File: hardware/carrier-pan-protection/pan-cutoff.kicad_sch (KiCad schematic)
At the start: 16 parts, among them Q1 100V N-MOS, Q2 100V N-MOS, U1 LTC4368IMS-2, U2 D42V55F12 / 5577

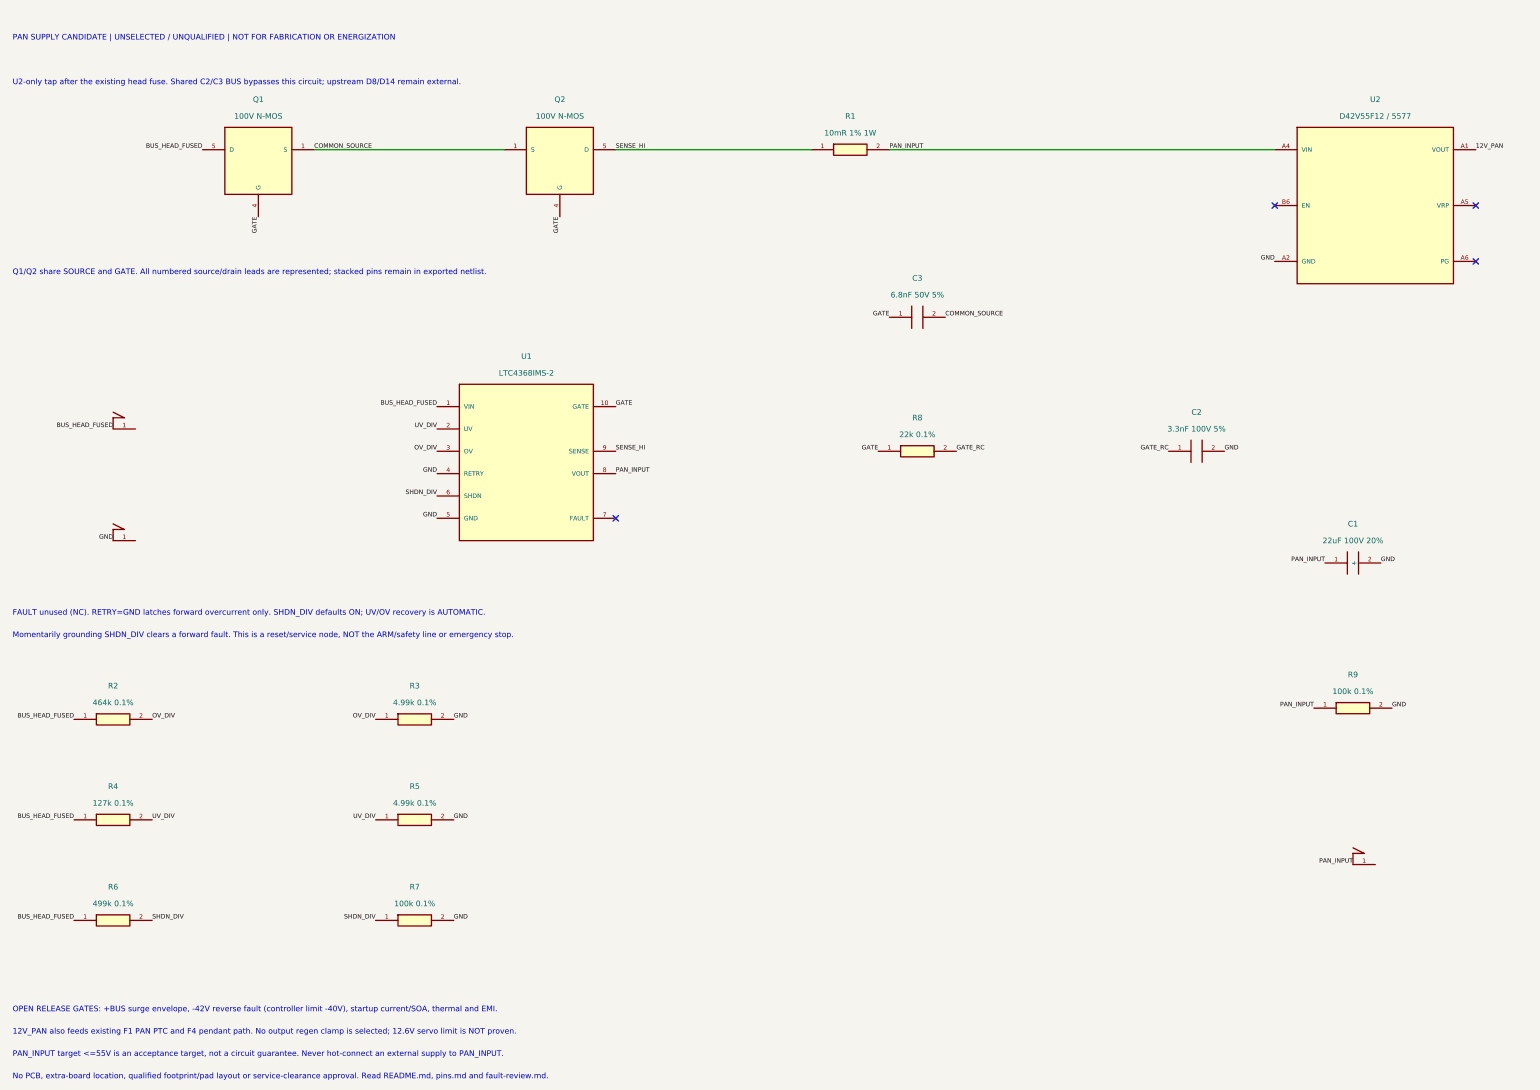
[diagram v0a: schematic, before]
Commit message: docs: draw auditable MOSFET and connected protection branches
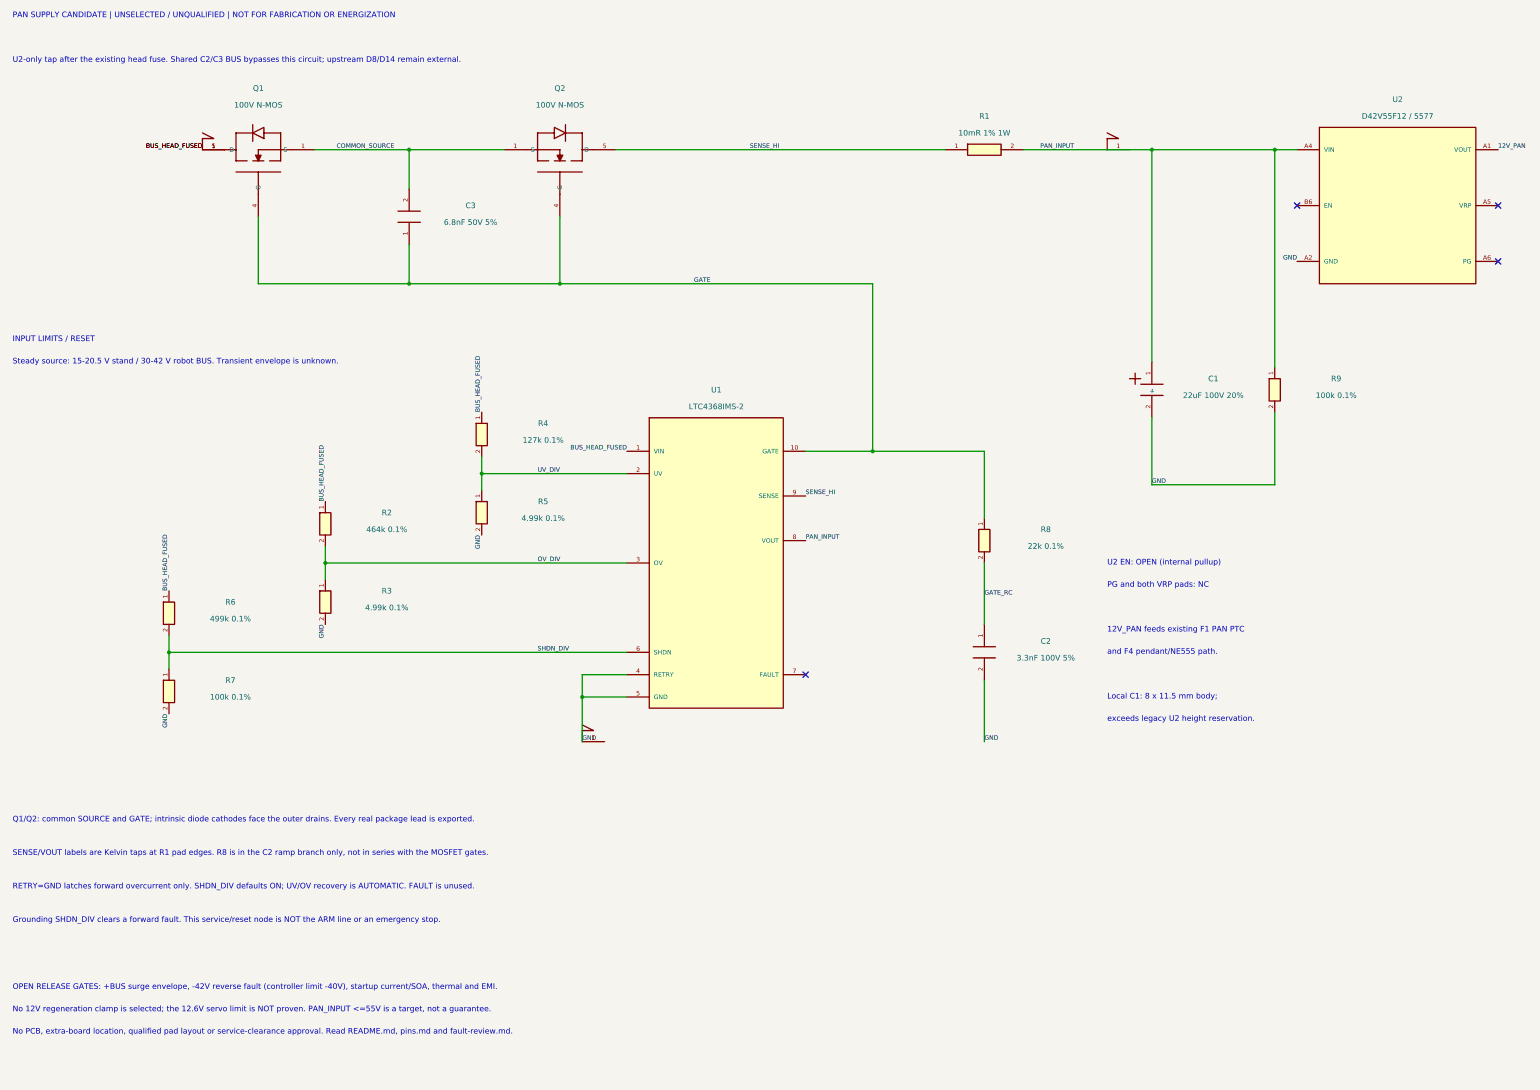
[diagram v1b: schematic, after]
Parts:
- C1: symbol Candidate:C_POL -> Candidate:C_POL_V
- C2: symbol Candidate:C -> Candidate:C_V
- C3: symbol Candidate:C -> Candidate:C_GS
- R2, R3, R4, R5, R6, R7, R8, R9: symbol Candidate:R -> Candidate:R_V
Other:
- note added: "12V_PAN feeds existing F1 PAN PTC"
- note added: "Grounding SHDN_DIV clears a forward fault. This service/reset node is NOT the ARM line or an emergency stop."
- note added: "INPUT LIMITS / RESET"
- note added: "Local C1: 8 x 11.5 mm body;"
- note added: "No 12V regeneration clamp is selected; the 12.6V servo limit is NOT proven. PAN_INPUT <=55V is a target, not a guarantee."
- note added: "No PCB, extra-board location, qualified pad layout or service-clearance approval. Read README.md, pins.md and fault-review.md."
- note added: "PG and both VRP pads: NC"
- note added: "Q1/Q2: common SOURCE and GATE; intrinsic diode cathodes face the outer drains. Every real package lead is exported."
- note added: "RETRY=GND latches forward overcurrent only. SHDN_DIV defaults ON; UV/OV recovery is AUTOMATIC. FAULT is unused."
- note added: "SENSE/VOUT labels are Kelvin taps at R1 pad edges. R8 is in the C2 ramp branch only, not in series with the MOSFET gates."
- note added: "Steady source: 15-20.5 V stand / 30-42 V robot BUS. Transient envelope is unknown."
- note added: "U2 EN: OPEN (internal pullup)"
- note added: "and F4 pendant/NE555 path."
- note added: "exceeds legacy U2 height reservation."
- note removed: "12V_PAN also feeds existing F1 PAN PTC and F4 pendant path. No output regen clamp is selected; 12.6V servo limit is NOT proven."
- note removed: "FAULT unused (NC). RETRY=GND latches forward overcurrent only. SHDN_DIV defaults ON; UV/OV recovery is AUTOMATIC."
- note removed: "Momentarily grounding SHDN_DIV clears a forward fault. This is a reset/service node, NOT the ARM/safety line or emergency stop."
- note removed: "No PCB, extra-board location, qualified footprint/pad layout or service-clearance approval. Read README.md, pins.md and fault-review.md."
- note removed: "PAN_INPUT target <=55V is an acceptance target, not a circuit guarantee. Never hot-connect an external supply to PAN_INPUT."
- note removed: "Q1/Q2 share SOURCE and GATE. All numbered source/drain leads are represented; stacked pins remain in exported netlist."
- moved on the sheet: C2, C3, R1, R2, R3, R4, R5, R6, R7, R8, R9, U1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

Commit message: Add reverse barrier and sequenced startup to PAN circuit candidate
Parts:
- added C4, C5: 100nF 100V 10% X7R, Capacitor_SMD:C_0805_2012Metric, symbol Candidate:C_V
- added C6, C7, C8: 47nF 100V 1%, Capacitor_SMD:C_1206_3216Metric, symbol Candidate:C_V
- added C9: 6.8nF 50V 5%, Capacitor_SMD:C_0805_2012Metric, symbol Candidate:C_V
- added D1: 200V series barrier, symbol Candidate:D_SERIES
- added D2: 200V negative clamp, symbol Candidate:D_CLAMP
- added R10: 20mR 1% 1W, Resistor_SMD:R_2512_6332Metric, symbol Candidate:R
- added R11: 100k 0.1%, Resistor_SMD:R_0805_2012Metric, symbol Candidate:R_V
- added R12: 150k 0.1%, Resistor_SMD:R_0805_2012Metric, symbol Candidate:R_V
- added R13: 10k 0.1%, Resistor_SMD:R_0805_2012Metric, symbol Candidate:R_V
- added R14: 499k 0.1%, Resistor_SMD:R_0805_2012Metric, symbol Candidate:R_V
- added U3: UV / OD active-low, symbol Candidate:TPS3760A012
- C2: value 3.3nF 100V 5% -> 47nF 100V 1%; footprint Capacitor_SMD:C_0805_2012Metric -> Capacitor_SMD:C_1206_3216Metric; MPN C0805C332J1GACTU -> C1206C473F1GECAUTO; Note ADI CGATE example value; actual U2 capacitance/inrush and S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 -> One of four parallel 47nF C0G ramp capacitors. Conditional 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
- Q1: Note Body diode anode=COMMON_SOURCE, cathode=BUS_HEAD_FUSED. Dra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 -> Body diode anode=COMMON_SOURCE, cathode=VIN_PROTECTED. Drai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
- R4: value 127k 0.1% -> 100k 0.1%; MPN TNPW0805127KBEEN -> TNPW0805100KBEEN; Note UV top; listed nonstock/reel order -> UV top; converter brownout is separately gated by U3
- U2: Note Project pad IDs A/B from manufacturer top view, see pins.md. EN left open uses internal pullup. VRP never used as input. PG unused; not a servo OVP. -> Project pad IDs A/B from manufacturer top view, see pins.md. EN driven by U3 UV supervisor; internal pullup retained. VRP never used as input. PG unused; not a servo OVP.
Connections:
- net BUS_HEAD_FUSED: now also D1.1 (A), D1.2 (A); no longer Q1.5 (D), Q1.6 (D), Q1.7 (D), Q1.8 (D), R2.1, R4.1, R6.1, U1.1 (VIN)
- net GATE_RC: now also C6.1, C7.1, C8.1
- net GND: now also C4.2, C5.2, C6.2, C7.2, C8.2, C9.2, D2.1 (A), D2.2 (A), R11.2, R13.2, U3.13 (GND), U3.8 (GND)
- net PAN_INPUT: now also C5.1, R10.2, R12.1, R14.1, U3.1 (VDD)
- net SENSE_HI: now also R10.1
- net PAN_ENABLE: now reaches U2.B6 (EN)
- net PAN_ENABLE: now also R14.2, U3.6 (RESET)
- new net EN_DELAY: C9.1, U3.9 (CTR)
- new net EN_SENSE: R12.2, R13.1, U3.3 (SENSE)
- new net VIN_PROTECTED: C4.1, D1.K, D2.K, Q1.5 (D), Q1.6 (D), Q1.7 (D), Q1.8 (D), R11.1, R2.1, R4.1, R6.1, U1.1 (VIN)
- no-connect marks 4 -> 11
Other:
- note added: "12V_PAN feeds existing F1 PAN PTC and F4 pendant/NE555 path."
- note added: "15-20.5 V stand / 30-42 V steady BUS. Source transients are unknown."
- note added: "CONVERTER STARTUP / BROWNOUT INHIBIT"
- note added: "Four C0G capacitors slow the U1 ramp; verify actual slew and Cin."
- note added: "INPUT WINDOW / FORWARD-FAULT LATCH"
- note added: "LOCAL NEGATIVE CLAMP / INPUT DECOUPLING"
- note added: "No extra PCB, power junction, external solder pad or carrier area allocated."
- note added: "OPEN GATES: hot insertion, source surge energy/impedance, diode/MOSFET SOA and thermal, converter startup/dropout/efficiency."
- note added: "Output regeneration/12.6 V servo limit, C1 ripple, solder/copper and physical fit remain unqualified. No energization authorized."
- note added: "PAN SUPPLY CANDIDATE B | UNSELECTED / UNQUALIFIED | NOT FOR FABRICATION OR ENERGIZATION"
- note added: "Place at U1 VIN/Q1 drain. Pulse and layout qualification remains open."
- note added: "R1 || R10 =6.667mOhm nominal. Both sense connections require shared Kelvin endpoints; no fuse coordination is established."
- note added: "R8 is in the ramp-capacitor branch only. Q1/Q2 share SOURCE/GATE; intrinsic diode cathodes face outer drains."
- note added: "RETRY=GND latches forward OC; UV/OV and U3 automatically recover. SHDN_DIV service reset is NOT ARM or emergency stop."
- note added: "See README.md, pins.md, fault-review.md and source-bound calculations. Zero ERC is connectivity evidence only."
- note added: "Series D1 blocks raw negative BUS; D2 limits local negative coupling."
- note added: "U2-only tap. Shared C2/C3 BUS bypasses this sheet; existing D8/D14 and head fuse receive NO protection credit."
- note added: "U3 actively pulls EN low until PAN_INPUT exceeds ~13 V."
- note added: "VIN_PROTECTED >= -2 V and PAN_INPUT <=55 V are test acceptance bounds,"
- note added: "not guaranteed waveforms. Charged-output VIN-VOUT >= -57 V in that envelope."
- note removed: "12V_PAN feeds existing F1 PAN PTC"
- note removed: "Grounding SHDN_DIV clears a forward fault. This service/reset node is NOT the ARM line or an emergency stop."
- note removed: "INPUT LIMITS / RESET"
- note removed: "Local C1: 8 x 11.5 mm body;"
- note removed: "No 12V regeneration clamp is selected; the 12.6V servo limit is NOT proven. PAN_INPUT <=55V is a target, not a guarantee."
- note removed: "No PCB, extra-board location, qualified pad layout or service-clearance approval. Read README.md, pins.md and fault-review.md."
- note removed: "OPEN RELEASE GATES: +BUS surge envelope, -42V reverse fault (controller limit -40V), startup current/SOA, thermal and EMI."
- note removed: "PAN SUPPLY CANDIDATE | UNSELECTED / UNQUALIFIED | NOT FOR FABRICATION OR ENERGIZATION"
- note removed: "PG and both VRP pads: NC"
- note removed: "Q1/Q2: common SOURCE and GATE; intrinsic diode cathodes face the outer drains. Every real package lead is exported."
- note removed: "RETRY=GND latches forward overcurrent only. SHDN_DIV defaults ON; UV/OV recovery is AUTOMATIC. FAULT is unused."
- note removed: "SENSE/VOUT labels are Kelvin taps at R1 pad edges. R8 is in the C2 ramp branch only, not in series with the MOSFET gates."
- note removed: "Steady source: 15-20.5 V stand / 30-42 V robot BUS. Transient envelope is unknown."
- note removed: "U2 EN: OPEN (internal pullup)"
- note removed: "U2-only tap after the existing head fuse. Shared C2/C3 BUS bypasses this circuit; upstream D8/D14 remain external."
- note removed: "and F4 pendant/NE555 path."
- note removed: "exceeds legacy U2 height reservation."

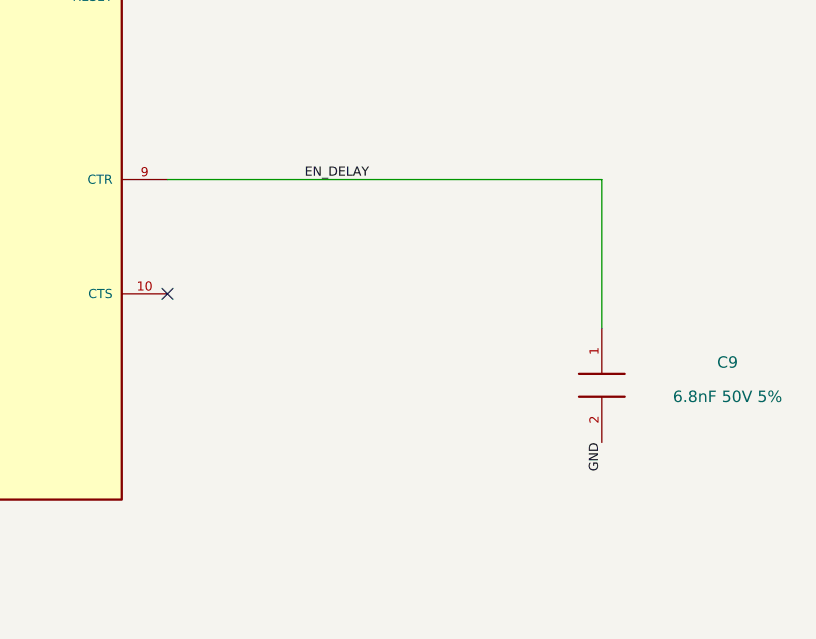
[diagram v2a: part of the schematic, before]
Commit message: Bind supervisor startup timing to an explicitly open CTR pin
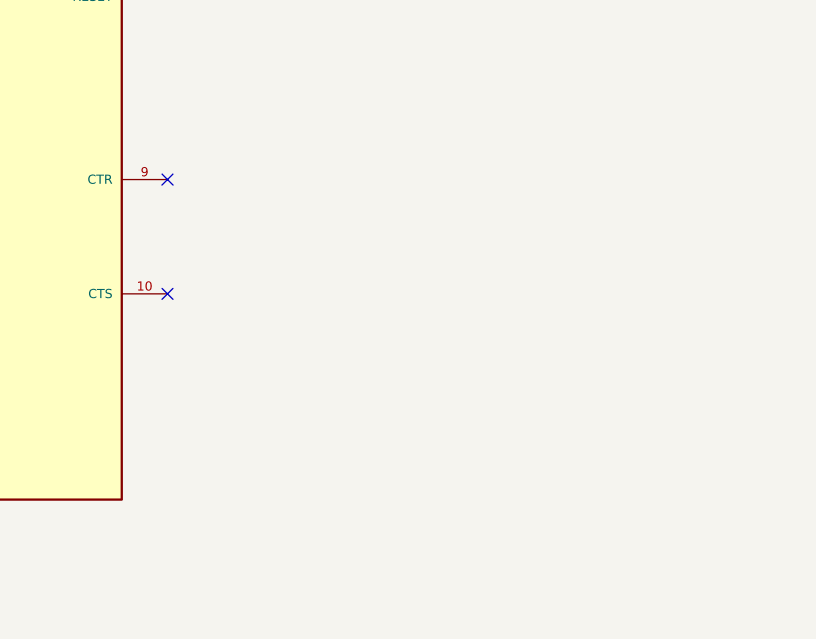
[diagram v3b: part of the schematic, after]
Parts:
- removed C9: 6.8nF 50V 5%, Capacitor_SMD:C_0805_2012Metric, symbol Candidate:C_V
- U3: Note A012 is adjustable UV with2% hysteresis and active-low open drain. E012 is OV, NOT a substitute. -> A012 is adjustable UV with2% hysteresis and active-low open drain. E012 is OV, NOT a substitute. CTR and CTS open; no added timing capacitor.
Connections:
- net EN_DELAY: no longer names the net of U3.9 (CTR)
- no-connect marks 11 -> 12
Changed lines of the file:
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@@
-	)
-	(symbol
-		(lib_id "Candidate:C_V")
-		(at 525.78 208.28 0)
-		(unit 1)
-		(exclude_from_sim no)
-		(in_bom yes)
-		(on_board yes)
-		(dnp no)
-		(property "Reference" "C9"
-			(at 539.75 205.74 0)
-			(effects
-				(font
-					(size 1.27 1.27)
-				)
-			)
-		)
-		(property "Value" "6.8nF 50V 5%"
-			(at 539.75 209.55 0)
-			(effects
-				(font
-					(size 1.27 1.27)
-				)
-			)
-		)
-		(property "Footprint" "Capacitor_SMD:C_0805_2012Metric"
-			(at 0 0 0)
-			(effects
-				(font
-					(size 1.27 1.27)
-				)
-				(hide yes)
-			)
-		)
-		(property "Datasheet" "https://yageogroup.com/content/datasheet/asset/file/KEM_C1003_C0G_SMD"
-			(at 0 0 0)
-			(effects
-				(font
-					(size 1.27 1.27)
-				)
-				(hide yes)
-			)
-		)
-		(property "MPN" "C0805C682J5GACTU"
-			(at 0 0 0)
-			(effects
-				(font
-					(size 1.27 1.27)
-				)
-				(hide yes)
-			)
-		)
-		(property "Status" "UNSELECTED / UNQUALIFIED CANDIDATE"
-			(at 0 0 0)
-			(effects
-				(font
-					(size 1.27 1.27)
-				)
-				(hide yes)
-			)
-		)
-		(property "Note" "U3 CTR release delay. CTS open for minimum assertion delay; no delay capacitor on SENSE."
-			(at 0 0 0)
-			(effects
-				(font
-					(size 1.27 1.27)
-				)
-				(hide yes)
-			)
-		)
-		(pin "1"
-		)
-		(pin "2"
-		)
-		(instances
-			(project "pan-cutoff"
-				(path "/a5073607-958b-514a-8360-0c680e339499"
-					(reference "C9")
-					(unit 1)
-				)
-			)
-		)
 	)
 	(symbol
@@
 			)
 		)
-		(property "Note" "A012 is adjustable UV with2% hysteresis and active-low open drain. E012 is OV, NOT a substitute."
+		(property "Note" "A012 is adjustable UV with2% hysteresis and active-low open drain. E012 is OV, NOT a substitute. CTR and CTS open; no added timing capacitor."
 			(at 0 0 0)
 			(effects
@@
 	)
 	(label "GND"
-		(at 525.78 214.63 270)
+		(at 436.88 208.28 180)
 		(effects
 			(font
@@
 		)
 	)
-	(label "GND"
-		(at 436.88 208.28 180)
-		(effects
-			(font
-				(size 1.016 1.016)
-			)
-			(justify right bottom)
-		)
+	(no_connect
+		(at 477.52 185.42)
 	)
 	(no_connect
@@
 		)
 	)
-	(wire
-		(pts
-			(xy 477.52 185.42)
-			(xy 525.78 185.42)
-		)
-		(stroke
-			(width 0)
-			(type default)
-		)
-	)
-	(wire
-		(pts
-			(xy 525.78 185.42)
-			(xy 525.78 201.93)
-		)
-		(stroke
-			(width 0)
-			(type default)
-		)
-	)
 	(label "COMMON_SOURCE"
 		(at 93.98 45.72 0)
@@
 		(effects
 			(font
-				(size 1.016 1.016)
-			)
-			(justify left bottom)
-		)
-	)
-	(label "EN_DELAY"
-		(at 492.76 185.42 0)
-		(effects
-			(font
